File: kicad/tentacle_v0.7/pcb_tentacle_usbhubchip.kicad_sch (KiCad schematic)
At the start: 34 parts, among them J301 USB_C_Receptacle_USB2.0, U302 USB2514B_Bi, Y301 24MHz

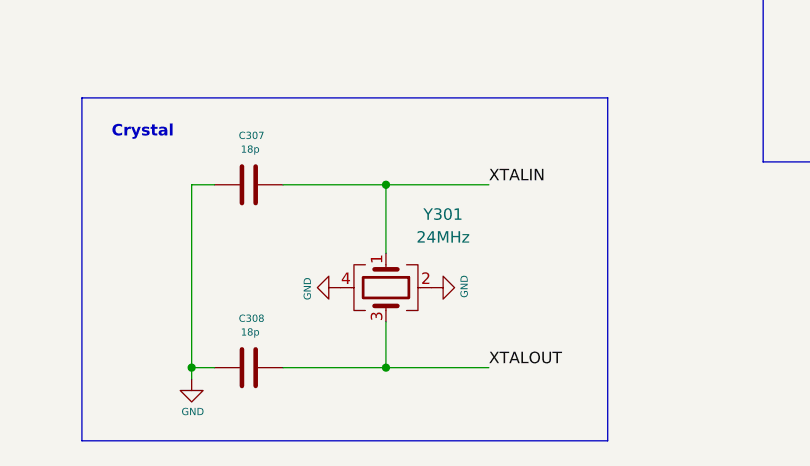
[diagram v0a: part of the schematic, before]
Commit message: Tentacle v0.7: Fix LEDs. Import new symbols and footprints
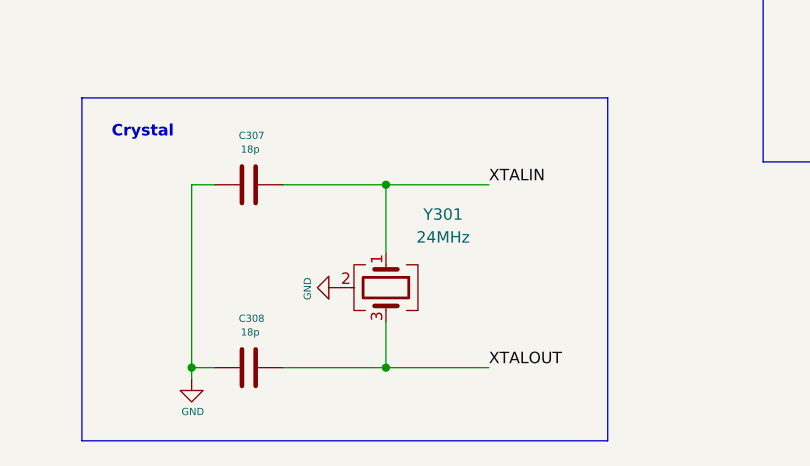
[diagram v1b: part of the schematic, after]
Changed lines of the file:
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@@
-	)
-	(symbol
-		(lib_id "power:GND")
-		(at 118.11 176.53 90)
-		(unit 1)
-		(exclude_from_sim no)
-		(in_bom yes)
-		(on_board yes)
-		(dnp no)
-		(property "Reference" "#PWR0316"
-			(at 124.46 176.53 0)
-			(effects
-				(font
-					(size 0.8 0.8)
-				)
-				(hide yes)
-			)
-		)
-		(property "Value" "GND"
-			(at 121.7422 176.403 0)
-			(effects
-				(font
-					(size 0.8 0.8)
-				)
-			)
-		)
-		(property "Footprint" ""
-			(at 118.11 176.53 0)
-			(effects
-				(font
-					(size 1.27 1.27)
-				)
-				(hide yes)
-			)
-		)
-		(property "Datasheet" ""
-			(at 118.11 176.53 0)
-			(effects
-				(font
-					(size 1.27 1.27)
-				)
-				(hide yes)
-			)
-		)
-		(property "Description" "Power symbol creates a global label with name \"GND\" , ground"
-			(at 118.11 176.53 0)
-			(effects
-				(font
-					(size 1.27 1.27)
-				)
-				(hide yes)
-			)
-		)
-		(pin "1"
-		)
-		(instances
-			(project "pcb_octohub"
-				(path "/35c47459-45a7-4753-acae-c8b47e7575e1/cff48fa5-514e-40a1-9e85-b0c2e53fd5a3"
-					(reference "#PWR0316")
-					(unit 1)
-				)
-			)
-			(project "pcb_octohub"
-				(path "/71f22cdd-d2e8-428f-a493-ba818011117e/cce2caaa-8f81-464b-90dc-a65beb95ce6e/905a4e11-6f14-4a1c-9cfb-b7581f2e2845"
-					(reference "#PWR01106")
-					(unit 1)
-				)
-			)
-		)
 	)
 	(symbol
@@
 			)
 		)
-		(property "Datasheet" "https://wmsc.lcsc.com/wmsc/upload/file/pdf/v2/lcsc/2403291504_YXC-X322524MOB4SI_C70590.pdf"
+		(property "Datasheet" "~"
 			(at 113.03 176.53 0)
 			(effects
@@
 			)
 		)
-		(property "Description" ""
+		(property "Description" "Light emitting diode"
 			(at 30.48 123.19 0)
 			(effects

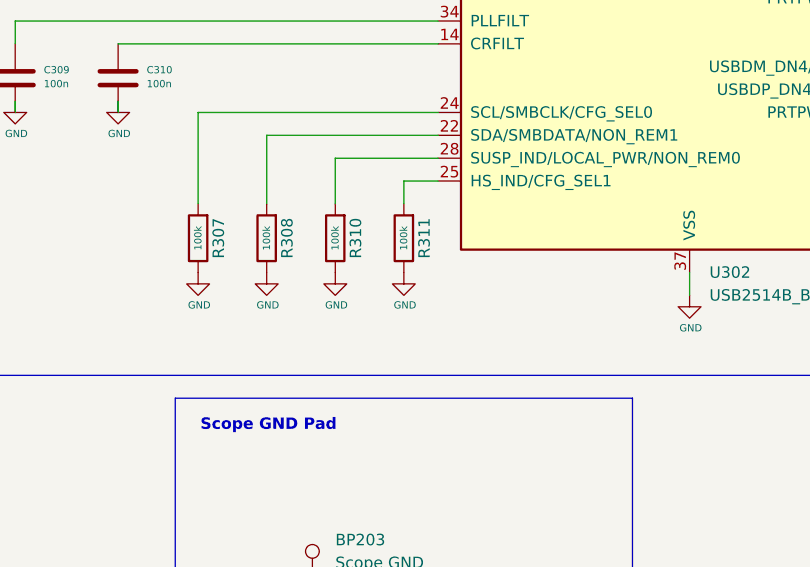
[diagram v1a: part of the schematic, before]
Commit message: Tentacle v0.7: HUB U302: CFG_SEL_1 0->1
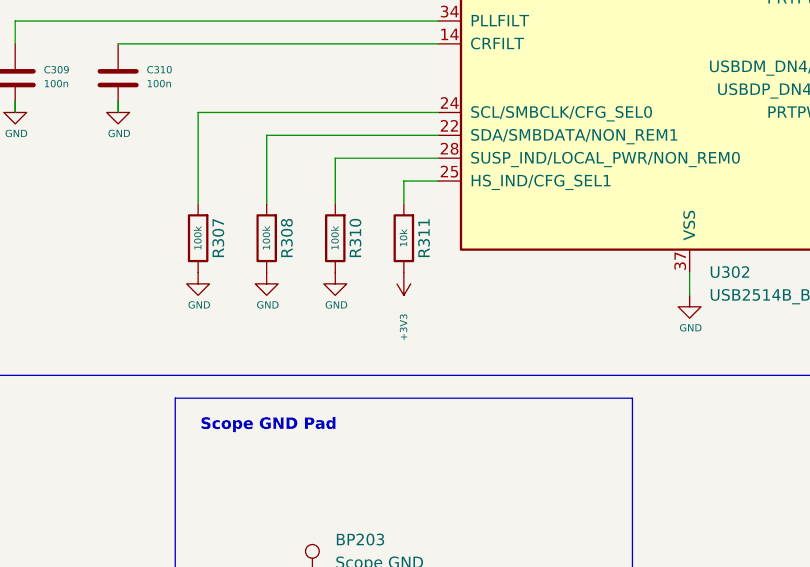
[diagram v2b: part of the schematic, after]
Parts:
- R311: value 100k -> 10k
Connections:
- net +3V3: now also R311.1
- net GND: no longer R311.1
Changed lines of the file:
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@@
 	)
 	(symbol
-		(lib_id "power:GND")
-		(at 180.34 114.3 0)
-		(unit 1)
-		(exclude_from_sim no)
-		(in_bom yes)
-		(on_board yes)
-		(dnp no)
-		(property "Reference" "#PWR0324"
-			(at 180.34 120.65 0)
-			(effects
-				(font
-					(size 0.8 0.8)
-				)
-				(hide yes)
-			)
-		)
-		(property "Value" "GND"
-			(at 180.467 117.9322 0)
+		(lib_id "power:+3V3")
+		(at 180.34 114.3 180)
+		(unit 1)
+		(exclude_from_sim no)
+		(in_bom yes)
+		(on_board yes)
+		(dnp no)
+		(property "Reference" "#PWR0241"
+			(at 180.34 110.49 0)
+			(effects
+				(font
+					(size 0.8 0.8)
+				)
+				(hide yes)
+			)
+		)
+		(property "Value" "+3V3"
+			(at 180.34 120.396 90)
 			(effects
 				(font
@@
 			)
 		)
-		(property "Description" "Power symbol creates a global label with name \"GND\" , ground"
+		(property "Description" "Power symbol creates a global label with name \"+3V3\""
 			(at 180.34 114.3 0)
 			(effects
@@
 			(project "pcb_tentacle"
 				(path "/35c47459-45a7-4753-acae-c8b47e7575e1/cff48fa5-514e-40a1-9e85-b0c2e53fd5a3"
-					(reference "#PWR0324")
+					(reference "#PWR0241")
 					(unit 1)
 				)
@@
 			)
 		)
-		(property "Value" "100k"
+		(property "Value" "10k"
 			(at 180.34 110.49 90)
 			(effects

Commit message: USB hub footprint: hole 0.2 mm -> 0.3 mm
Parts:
- U302: footprint Package_DFN_QFN:Texas_RHH0036C_VQFN-36-1EP_6x6mm_P0.5mm_EP4.4x4.4mm_ThermalVias -> 00_project_library:Texas_RHH0036C_VQFN-36-1EP_6x6mm_P0.5mm_EP4.4x4.4mm_ThermalVias
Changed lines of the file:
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@@
 			)
 		)
-		(property "Footprint" "Package_DFN_QFN:Texas_RHH0036C_VQFN-36-1EP_6x6mm_P0.5mm_EP4.4x4.4mm_ThermalVias"
+		(property "Footprint" "00_project_library:Texas_RHH0036C_VQFN-36-1EP_6x6mm_P0.5mm_EP4.4x4.4mm_ThermalVias"
 			(at 245.11 114.3 0)
 			(effects

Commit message: Tentacle: v0.7.1
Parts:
- R311: value 10k -> 100k
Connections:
- net +3V3: no longer R311.1
- net GND: now also R311.1
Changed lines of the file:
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@@
 	(title_block
 		(title "Octoprobe tentacle")
-		(date "2026-01-20")
-		(rev "0.7")
+		(date "2026-02-18")
+		(rev "0.7.1")
 		(company "Hans Märki, Märki Informatik")
 		(comment 1 "The MIT License (MIT)")
@@
 	)
 	(symbol
-		(lib_id "power:+3V3")
-		(at 180.34 114.3 180)
-		(unit 1)
-		(exclude_from_sim no)
-		(in_bom yes)
-		(on_board yes)
-		(dnp no)
-		(property "Reference" "#PWR0241"
-			(at 180.34 110.49 0)
-			(effects
-				(font
-					(size 0.8 0.8)
-				)
-				(hide yes)
-			)
-		)
-		(property "Value" "+3V3"
-			(at 180.34 120.396 90)
-			(effects
-				(font
-					(size 0.8 0.8)
-				)
-			)
-		)
-		(property "Footprint" ""
-			(at 180.34 114.3 0)
-			(effects
-				(font
-					(size 1.27 1.27)
-				)
-				(hide yes)
-			)
-		)
-		(property "Datasheet" ""
-			(at 180.34 114.3 0)
-			(effects
-				(font
-					(size 1.27 1.27)
-				)
-				(hide yes)
-			)
-		)
-		(property "Description" "Power symbol creates a global label with name \"+3V3\""
-			(at 180.34 114.3 0)
-			(effects
-				(font
-					(size 1.27 1.27)
-				)
-				(hide yes)
-			)
-		)
-		(pin "1"
-		)
-		(instances
-			(project "pcb_tentacle"
-				(path "/35c47459-45a7-4753-acae-c8b47e7575e1/cff48fa5-514e-40a1-9e85-b0c2e53fd5a3"
-					(reference "#PWR0241")
-					(unit 1)
-				)
-			)
-		)
-	)
-	(symbol
 		(lib_id "Device:R")
 		(at 254 41.91 0)
@@
 	(symbol
 		(lib_id "power:GND")
+		(at 180.34 114.3 0)
+		(unit 1)
+		(exclude_from_sim no)
+		(in_bom yes)
+		(on_board yes)
+		(dnp no)
+		(property "Reference" "#PWR0241"
+			(at 180.34 120.65 0)
+			(effects
+				(font
+					(size 0.8 0.8)
+				)
+				(hide yes)
+			)
+		)
+		(property "Value" "GND"
+			(at 180.467 117.9322 0)
+			(effects
+				(font
+					(size 0.8 0.8)
+				)
+			)
+		)
+		(property "Footprint" ""
+			(at 180.34 114.3 0)
+			(effects
+				(font
+					(size 1.27 1.27)
+				)
+				(hide yes)
+			)
+		)
+		(property "Datasheet" ""
+			(at 180.34 114.3 0)
+			(effects
+				(font
+					(size 1.27 1.27)
+				)
+				(hide yes)
+			)
+		)
+		(property "Description" "Power symbol creates a global label with name \"GND\" , ground"
+			(at 180.34 114.3 0)
+			(effects
+				(font
+					(size 1.27 1.27)
+				)
+				(hide yes)
+			)
+		)
+		(pin "1"
+		)
+		(instances
+			(project "pcb_tentacle"
+				(path "/35c47459-45a7-4753-acae-c8b47e7575e1/cff48fa5-514e-40a1-9e85-b0c2e53fd5a3"
+					(reference "#PWR0241")
+					(unit 1)
+				)
+			)
+		)
+	)
+	(symbol
+		(lib_id "power:GND")
 		(at 157.48 114.3 0)
 		(unit 1)
@@
 			)
 		)
-		(property "Value" "10k"
+		(property "Value" "100k"
 			(at 180.34 110.49 90)
 			(effects
